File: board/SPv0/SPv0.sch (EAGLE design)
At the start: 69 parts, among them IC1 S34ML0XG1, IC2 F55[0/1]X---PT48, IC3 TL084D, Q1 12MHz, T1 n3904, T2 n3904, T3 n3906, T4 n3906, T5 n3906

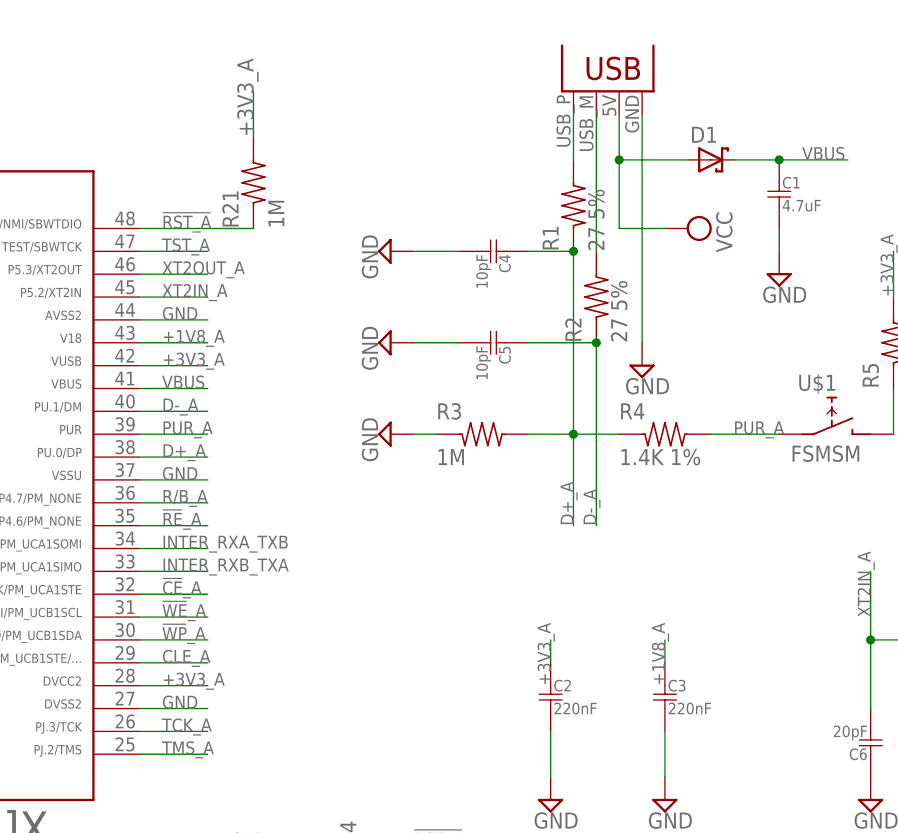
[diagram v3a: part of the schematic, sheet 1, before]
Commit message: added schottky diode to library fixed up led symbol swapping in sod123 diode for d1
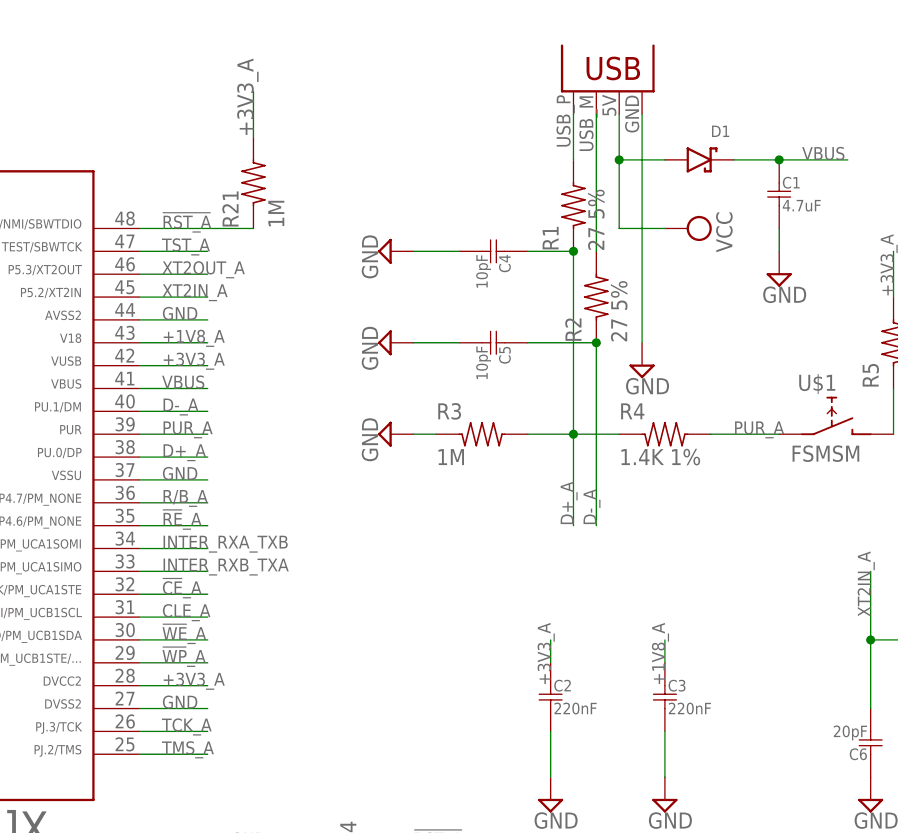
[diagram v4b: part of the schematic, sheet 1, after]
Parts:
- D1: device diode:SCHOTTKY-DIODESMD -> Passives:D-SCHOTTKY
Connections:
- net !WE!_A: now also IC2.30; no longer IC2.31
- net !WP!_A: now also IC2.29; no longer IC2.30
- net CLE_A: now also IC2.31; no longer IC2.29
- net VBUS: now also D1.CATHODE; no longer D1.C
- net VCC: now also D1.ANODE; no longer D1.A
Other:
- moved on the sheet: D1
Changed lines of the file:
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@@
 <part name="R1" library="Passives" deviceset="R" device="0805" value="27 5%"/>
 <part name="R2" library="Passives" deviceset="R" device="0805" value="27 5%"/>
-<part name="D1" library="diode" deviceset="SCHOTTKY-DIODE" device="SMD"/>
 <part name="Q1" library="Passives" deviceset="CRYSTAL" device="CSM-3X" value="12MHz"/>
 <part name="U$1" library="Passives" deviceset="FSMSM" device=""/>
@@
 <part name="U$10" library="Passives" deviceset="R" device="0805" value="130"/>
 <part name="U$11" library="Passives" deviceset="R" device="0805" value="130"/>
+<part name="D1" library="Passives" deviceset="D-SCHOTTKY" device=""/>
 </parts>
 <sheets>
@@
 <instance part="R1" gate="G$1" x="121.92" y="119.38" rot="R90"/>
 <instance part="R2" gate="G$1" x="124.46" y="109.22" rot="R90"/>
-<instance part="D1" gate="G$1" x="137.16" y="124.46"/>
 <instance part="Q1" gate="G$1" x="162.56" y="71.12"/>
 <instance part="U$1" gate="G$1" x="149.86" y="96.52"/>
@@
 <instance part="U$10" gate="G$1" x="-2.54" y="106.68"/>
 <instance part="U$11" gate="G$1" x="-2.54" y="101.6"/>
+<instance part="D1" gate="G$1" x="137.16" y="124.46"/>
 </instances>
 <busses>
@@
 </segment>
 <segment>
-<pinref part="D1" gate="G$1" pin="C"/>
-<wire x1="139.7" y1="124.46" x2="144.78" y2="124.46" width="0.1524" layer="91"/>
 <label x="147.32" y="124.46" size="1.4224" layer="95"/>
 <pinref part="C1" gate="G$1" pin="1"/>
 <wire x1="144.78" y1="124.46" x2="152.4" y2="124.46" width="0.1524" layer="91"/>
+<pinref part="D1" gate="G$1" pin="CATHODE"/>
+<wire x1="139.7" y1="124.46" x2="144.78" y2="124.46" width="0.1524" layer="91"/>
 <junction x="144.78" y="124.46"/>
 </segment>
@@
 <net name="!WE!_A" class="0">
 <segment>
+<pinref part="IC1" gate="G$1" pin="!WE"/>
+<wire x1="195.58" y1="91.44" x2="187.96" y2="91.44" width="0.1524" layer="91"/>
+<label x="187.96" y="91.44" size="1.4224" layer="95"/>
+</segment>
+<segment>
+<pinref part="IC2" gate="G$1" pin="30"/>
+<wire x1="73.66" y1="71.12" x2="81.28" y2="71.12" width="0.1524" layer="91"/>
+<label x="76.2" y="71.12" size="1.4224" layer="95"/>
+</segment>
+</net>
+<net name="!WP!_A" class="0">
+<segment>
+<pinref part="IC1" gate="G$1" pin="!WP"/>
+<wire x1="195.58" y1="88.9" x2="187.96" y2="88.9" width="0.1524" layer="91"/>
+<label x="187.96" y="88.9" size="1.4224" layer="95"/>
+</segment>
+<segment>
+<pinref part="IC2" gate="G$1" pin="29"/>
+<wire x1="73.66" y1="68.58" x2="81.28" y2="68.58" width="0.1524" layer="91"/>
+<label x="76.2" y="68.58" size="1.4224" layer="95"/>
+</segment>
+</net>
+<net name="CLE_A" class="0">
+<segment>
+<pinref part="IC1" gate="G$1" pin="CLE"/>
+<wire x1="195.58" y1="83.82" x2="187.96" y2="83.82" width="0.1524" layer="91"/>
+<label x="187.96" y="83.82" size="1.4224" layer="95"/>
+</segment>
+<segment>
 <pinref part="IC2" gate="G$1" pin="31"/>
 <wire x1="73.66" y1="73.66" x2="81.28" y2="73.66" width="0.1524" layer="91"/>
 <label x="76.2" y="73.66" size="1.4224" layer="95"/>
 </segment>
-<segment>
-<pinref part="IC1" gate="G$1" pin="!WE"/>
-<wire x1="195.58" y1="91.44" x2="187.96" y2="91.44" width="0.1524" layer="91"/>
-<label x="187.96" y="91.44" size="1.4224" layer="95"/>
-</segment>
-</net>
-<net name="!WP!_A" class="0">
-<segment>
-<pinref part="IC2" gate="G$1" pin="30"/>
-<wire x1="73.66" y1="71.12" x2="81.28" y2="71.12" width="0.1524" layer="91"/>
-<label x="76.2" y="71.12" size="1.4224" layer="95"/>
-</segment>
-<segment>
-<pinref part="IC1" gate="G$1" pin="!WP"/>
-<wire x1="195.58" y1="88.9" x2="187.96" y2="88.9" width="0.1524" layer="91"/>
-<label x="187.96" y="88.9" size="1.4224" layer="95"/>
-</segment>
-</net>
-<net name="CLE_A" class="0">
-<segment>
-<pinref part="IC2" gate="G$1" pin="29"/>
-<wire x1="73.66" y1="68.58" x2="81.28" y2="68.58" width="0.1524" layer="91"/>
-<label x="76.2" y="68.58" size="1.4224" layer="95"/>
-</segment>
-<segment>
-<pinref part="IC1" gate="G$1" pin="CLE"/>
-<wire x1="195.58" y1="83.82" x2="187.96" y2="83.82" width="0.1524" layer="91"/>
-<label x="187.96" y="83.82" size="1.4224" layer="95"/>
-</segment>
 </net>
 <net name="ALE_A" class="0">
@@
 <pinref part="JP1" gate="G$1" pin="VBUS"/>
 <wire x1="127" y1="129.54" x2="127" y2="124.46" width="0.1524" layer="91"/>
-<pinref part="D1" gate="G$1" pin="A"/>
-<wire x1="127" y1="124.46" x2="134.62" y2="124.46" width="0.1524" layer="91"/>
 <wire x1="127" y1="124.46" x2="127" y2="116.84" width="0.1524" layer="91"/>
-<junction x="127" y="124.46"/>
 <pinref part="SUPPLY27" gate="G$1" pin="VCC"/>
 <wire x1="127" y1="116.84" x2="132.08" y2="116.84" width="0.1524" layer="91"/>
-</segment>
-</net>
+<pinref part="D1" gate="G$1" pin="ANODE"/>
+<wire x1="132.08" y1="124.46" x2="127" y2="124.46" width="0.1524" layer="91"/>
+<junction x="127" y="124.46"/>
+</segment>
+</net>

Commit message: 1/2 board w/ new rng done. needs test points, confirm switch
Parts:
- removed C10: 4.7u, rcl:C-EUC0805
- removed C11: 120pF, rcl:C-EUC0603
- removed C12: 4.7uF, rcl:C-EUC0805
- removed C13: 2.2uF, rcl:C-EUC0603
- removed C8, C9: 0.47u, rcl:C-EUC0805
- removed D2, D3: 1n4148, zetex:DSOD323
- removed D4: (no value), diode:DIODE-SOD123
- removed IC3: TL084D, linear:TL084D
- removed R10: 1M, rcl:R-US_R0603
- removed R11, R12: 100K, rcl:R-US_R0603
- removed R13: 1.2K, rcl:R-US_R0603
- removed R14, R15: 10K, rcl:R-US_R0603
- removed R16, R17: 5K, rcl:R-US_R0603
- removed R18: 51K, rcl:R-US_R0603
- removed R19: 205K, rcl:R-US_R0603
- removed R20: 13.3K, rcl:R-US_R0603
- removed R8: 12K, rcl:R-US_R0603
- removed R9: 47K, rcl:R-US_R0603
- removed T1, T2: n3904, transistor:MMBT3904LT1-NPN-SOT23-BEC
- removed T3, T4, T5: n3906, transistor:MMBT3906LT1-PNP-SOT23-BEC
- removed TP2: PTR1PAD1-13, testpad:PTR1PAD1-13
- removed U$2: LM27313, rng:LM27313
- removed U$3: 10uH, rng:CB2518
- added IC4: 74LS14D, 74xx-us:74LS14D
- R6: value 150K -> 1.4k; device rcl:R-US_R0603 -> Passives:R0805
- R7: value 1M -> 1.4k; device rcl:R-US_R0603 -> Passives:R0805
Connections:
- removed net AOUT: IC3B.OUT, R9.2, T5.B
- removed net N$11: IC3B.+IN, R10.1
- removed net N$12: C10.1, IC3C.+IN, R11.1, R12.2
- removed net N$13: D3.C, R14.2, T3.B
- removed net N$14: D2.C, D3.A
- removed net N$15: R13.1, T3.E
- removed net N$16: T3.C, T4.E, T5.E
- removed net N$17: R15.2, T4.C
- removed net N$18: R17.1, T5.C
- removed net N$20: D4.A, U$2.SW, U$3.P$2
- removed net N$21: C11.2, R19.2, R20.1, U$2.FB
- removed net VDD: C11.1, C12.1, D2.A, D4.C, IC3P.V+, R11.2, R13.2, R19.1, R6.2
- removed net VREF: IC3C.-IN, IC3C.OUT, R10.2, R7.2, T4.B
- net !VDD_SHDN!: no longer R18.2, U$2.!SHDN!
- net DOUT: now also R6.1, R7.2; no longer R16.1, R17.2, TP2.TP
- net GND: now also IC4P.GND, R7.1; no longer C10.2, C12.2, C13.1, IC3D.+IN, IC3D.-IN, IC3P.V-, R12.1, R14.1, R15.1, R16.2, R18.1, R20.2, T2.E, U$2.GND
- net N$10: now also IC4F.O, R6.2; no longer IC3B.-IN, R8.2, R9.1
- net N$5: now also IC4A.O, IC4B.I; no longer C8.1, R6.1, T1.E, T2.C
- net N$6: now also IC4B.O, IC4C.I; no longer T1.B, T2.B
- net N$7: now also IC4C.O, IC4D.I; no longer C8.2, IC3A.+IN, R7.1
- net N$8: now also IC4D.O, IC4E.I; no longer C9.1, IC3A.-IN, IC3A.OUT
- net N$9: now also IC4A.I, IC4E.O, IC4F.I; no longer C9.2, R8.1
- net VCC: now also IC4P.VCC; no longer C13.2, U$2.VIN, U$3.P$1

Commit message: halfboard v1 done!
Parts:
- added SJ1: (no value), jumper:SJW
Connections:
- new net N$11: R4.2, SJ1.1
- new net SW_A: IC2.4, U$1.B
- net GND: now also U$1.A1
- net N$4: now also SJ1.2; no longer U$1.B
- net PUR_A: no longer R4.2, U$1.A1
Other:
- note removed: "RNG"
- moved on the sheet: U$1
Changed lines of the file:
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@@
 <part name="R7" library="Passives" deviceset="R" device="0805" value="1.4k"/>
 <part name="SUPPLY13" library="supply2" deviceset="GND" device=""/>
+<part name="SJ1" library="jumper" deviceset="SJ" device="W"/>
+<part name="SUPPLY14" library="supply2" deviceset="GND" device=""/>
 </parts>
 <sheets>
 <sheet>
 <plain>
-<text x="17.78" y="99.06" size="1.4224" layer="91">RNG</text>
-<text x="17.78" y="96.52" size="1.4224" layer="91">RNG</text>
-<text x="17.78" y="106.68" size="1.4224" layer="91">RNG</text>
-<text x="17.78" y="104.14" size="1.4224" layer="91">RNG</text>
 </plain>
 <instances>
@@
 <instance part="R2" gate="G$1" x="124.46" y="109.22" rot="R90"/>
 <instance part="Q1" gate="G$1" x="162.56" y="71.12"/>
-<instance part="U$1" gate="G$1" x="149.86" y="96.52"/>
+<instance part="U$1" gate="G$1" x="27.94" y="35.56"/>
 <instance part="R3" gate="G$1" x="111.76" y="93.98"/>
 <instance part="SUPPLY10" gate="GND" x="101.6" y="93.98" rot="R270"/>
@@
 <instance part="U$11" gate="G$1" x="-2.54" y="101.6"/>
 <instance part="D1" gate="G$1" x="137.16" y="124.46"/>
+<instance part="SJ1" gate="1" x="149.86" y="93.98"/>
+<instance part="SUPPLY14" gate="GND" x="15.24" y="33.02" rot="R270"/>
 </instances>
 <busses>
@@
 <pinref part="C14" gate="G$1" pin="2"/>
 <wire x1="-2.54" y1="86.36" x2="2.54" y2="86.36" width="0.1524" layer="91"/>
+</segment>
+<segment>
+<pinref part="SUPPLY14" gate="GND" pin="GND"/>
+<pinref part="U$1" gate="G$1" pin="A1"/>
+<wire x1="17.78" y1="33.02" x2="22.86" y2="33.02" width="0.1524" layer="91"/>
 </segment>
 </net>
@@
 <label x="76.2" y="93.98" size="1.4224" layer="95"/>
 </segment>
-<segment>
-<pinref part="R4" gate="G$1" pin="2"/>
-<pinref part="U$1" gate="G$1" pin="A1"/>
-<wire x1="137.16" y1="93.98" x2="144.78" y2="93.98" width="0.1524" layer="91"/>
-<label x="139.7" y="93.98" size="1.4224" layer="95"/>
-</segment>
-</net>
-<net name="N$4" class="0">
-<segment>
-<pinref part="U$1" gate="G$1" pin="B"/>
-<pinref part="R5" gate="G$1" pin="1"/>
-<wire x1="157.48" y1="93.98" x2="157.48" y2="99.06" width="0.1524" layer="91"/>
-</segment>
 </net>
 <net name="TDO_A" class="0">
@@
 </segment>
 </net>
+<net name="N$4" class="0">
+<segment>
+<pinref part="R5" gate="G$1" pin="1"/>
+<wire x1="157.48" y1="99.06" x2="157.48" y2="93.98" width="0.1524" layer="91"/>
+<pinref part="SJ1" gate="1" pin="2"/>
+<wire x1="157.48" y1="93.98" x2="154.94" y2="93.98" width="0.1524" layer="91"/>
+</segment>
+</net>
+<net name="N$11" class="0">
+<segment>
+<pinref part="SJ1" gate="1" pin="1"/>
+<pinref part="R4" gate="G$1" pin="2"/>
+<wire x1="144.78" y1="93.98" x2="137.16" y2="93.98" width="0.1524" layer="91"/>
+</segment>
+</net>
+<net name="SW_A" class="0">
+<segment>
+<pinref part="U$1" gate="G$1" pin="B"/>
+<wire x1="35.56" y1="33.02" x2="43.18" y2="33.02" width="0.1524" layer="91"/>
+<label x="38.1" y="33.02" size="1.778" layer="95"/>
+</segment>
+<segment>
+<pinref part="IC2" gate="G$1" pin="4"/>
+<wire x1="22.86" y1="109.22" x2="15.24" y2="109.22" width="0.1524" layer="91"/>
+<label x="15.24" y="109.22" size="1.778" layer="95"/>
+</segment>
+</net>
